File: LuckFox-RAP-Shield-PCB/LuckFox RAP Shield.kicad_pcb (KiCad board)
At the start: 2 copper layers, 21.3 x 28.4 mm, 4 parts, among them J1 LuckFox_Pico_Mini_Connector, J2 External_5V_Input_from_Buck_M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, U2 W5500_Ethernet_Module_DNP_on_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

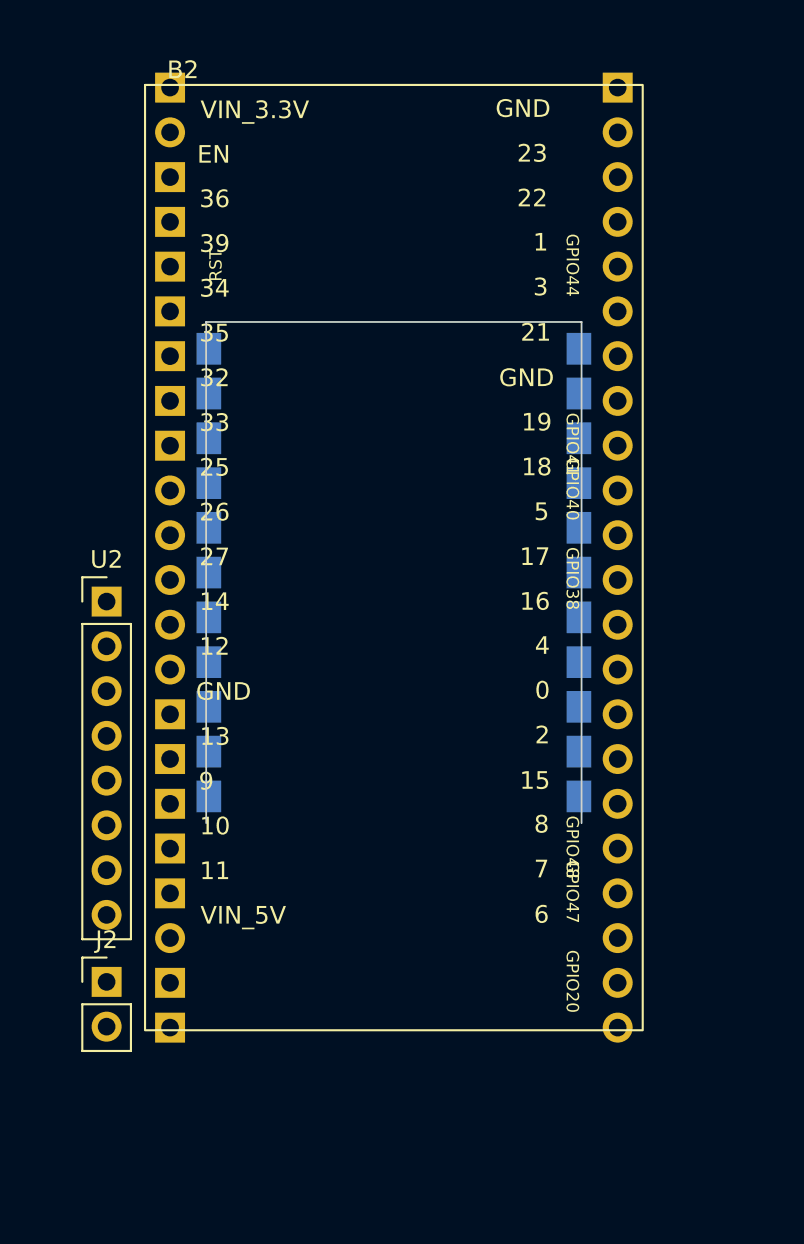
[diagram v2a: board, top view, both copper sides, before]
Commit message: Re-center J1 for the corrected LuckFox footprint dimensions
J1 local center shifted to (10.5, 13.4) with the new 21x26.8mm body.
Re-centered at (124.8, 96.04) using B2's current position; also
picked up that J1 had moved again in your own session.
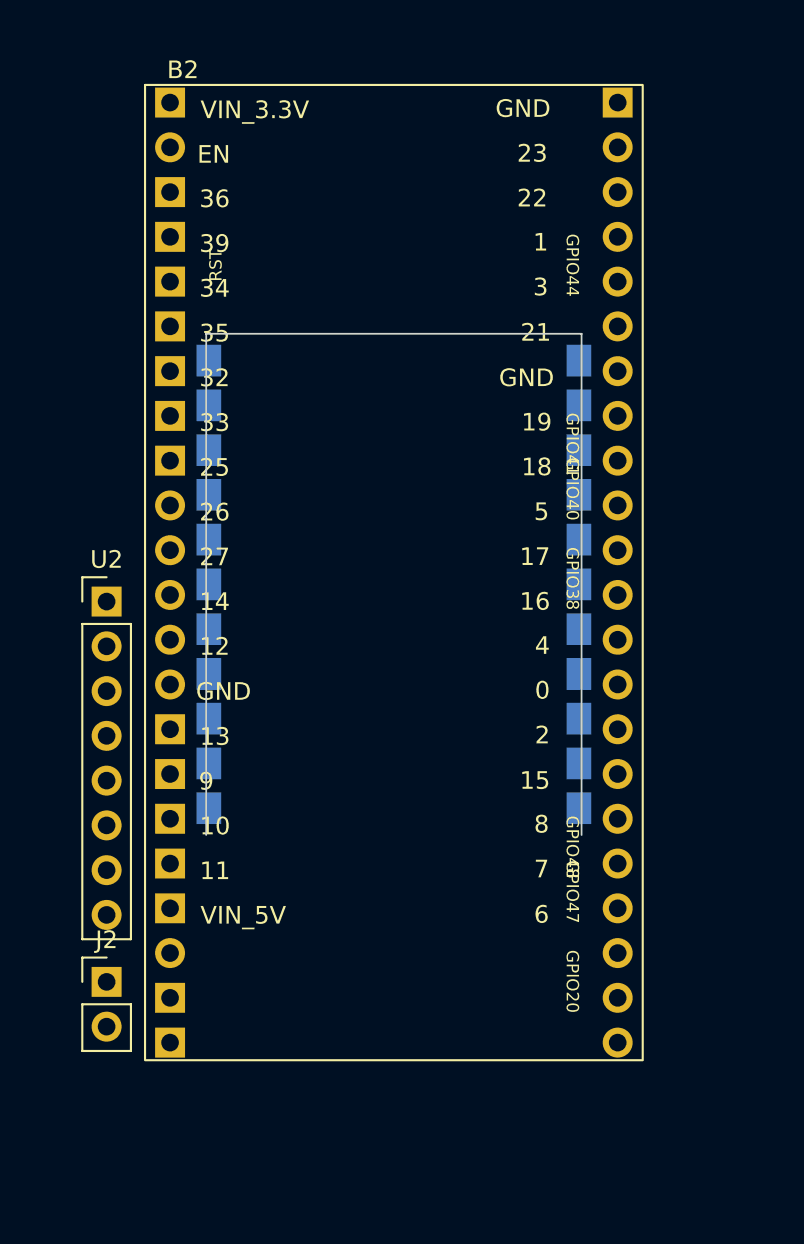
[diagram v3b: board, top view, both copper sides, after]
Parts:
- moved J1 0.67 mm to (124.8, 96.0)
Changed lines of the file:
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@@
 		(layer "F.Cu")
 		(at 121.33 81.92)
-		(descr "Real ESP32-S3-WROOM-1 DevKitC-1 dual-USB-C variant, 44 pins (22/row), 2.54mm pitch, 25.40mm row spacing (1.27mm inset from each edge on a 27.94mm-wide board). Pin labels and this shield's schematic-pin-number mapping are per the board's own silkscreen GPIO numbers -- confirmed against a full pinout diagram. Board length equals the pin-to-pin span exactly (53.34mm, 21 gaps x 2.54mm), zero top/bottom margin, per direct user measurement -- first pin row is flush with the top edge, last pin row flush with the bottom edge.")
+		(descr "Real ESP32-S3-WROOM-1 DevKitC-1 dual-USB-C variant, 44 pins (22/row), 2.54mm pitch, 25.40mm row spacing (1.27mm inset from each edge on a 27.94mm-wide board). Pin labels and this shield's schematic-pin-number mapping are per the board's own silkscreen GPIO numbers -- confirmed against a full pinout diagram. Board length is the pin-to-pin span (53.34mm, 21 gaps x 2.54mm, per direct user measurement) plus 0.85mm margin on each end (half the 1.7mm pad size) so the through-hole pads are physically whole rather than clipped by the board edge -- this is a normal pin-header board, not castellated.")
 		(property "Reference" "B2"
 			(at 2 -1 0)
@@
 		(fp_rect
 			(start -0.15 -0.15)
-			(end 28.09 53.49)
+			(end 28.09 55.19)
 			(stroke
 				(width 0.12)
@@
 		(fp_rect
 			(start -0.4 -0.4)
-			(end 28.34 53.74)
+			(end 28.34 55.44)
 			(stroke
 				(width 0.05)
@@
 		(fp_rect
 			(start 0 0)
-			(end 27.94 53.34)
+			(end 27.94 55.04)
 			(stroke
 				(width 0.1)
@@
 		)
 		(pad "1" thru_hole rect
-			(at 1.27 50.8 90)
+			(at 1.27 51.65 90)
 			(size 1.7 1.7)
 			(drill 1)
@@
 		)
 		(pad "2" thru_hole rect
-			(at 1.27 0 90)
+			(at 1.27 0.85 90)
 			(size 1.7 1.7)
 			(drill 1)
@@
 		)
 		(pad "3" thru_hole rect
-			(at 1.27 53.34 90)
+			(at 1.27 54.19 90)
 			(size 1.7 1.7)
 			(drill 1)
@@
 		)
 		(pad "3V3_B" thru_hole circle
-			(at 1.27 2.54 90)
+			(at 1.27 3.39 90)
 			(size 1.7 1.7)
 			(drill 1)
@@
 		)
 		(pad "4" thru_hole rect
-			(at 1.27 5.08 90)
+			(at 1.27 5.93 90)
 			(size 1.7 1.7)
 			(drill 1)
@@
 		)
 		(pad "5" thru_hole rect
-			(at 1.27 7.62 90)
+			(at 1.27 8.47 90)
 			(size 1.7 1.7)
 			(drill 1)
@@
 		)
 		(pad "6" thru_hole rect
-			(at 1.27 10.16 90)
+			(at 1.27 11.01 90)
 			(size 1.7 1.7)
 			(drill 1)
@@
 		)
 		(pad "7" thru_hole rect
-			(at 1.27 12.7 90)
+			(at 1.27 13.55 90)
 			(size 1.7 1.7)
 			(drill 1)
@@
 		)
 		(pad "8" thru_hole rect
-			(at 1.27 15.24 90)
+			(at 1.27 16.09 90)
 			(size 1.7 1.7)
 			(drill 1)
@@
 		)
 		(pad "9" thru_hole rect
-			(at 1.27 35.56 90)
+			(at 1.27 36.41 90)
 			(size 1.7 1.7)
 			(drill 1)
@@
 		)
 		(pad "10" thru_hole rect
-			(at 1.27 38.1 90)
+			(at 1.27 38.95 90)
 			(size 1.7 1.7)
 			(drill 1)
@@
 		)
 		(pad "11" thru_hole rect
-			(at 1.27 40.64 90)
+			(at 1.27 41.49 90)
 			(size 1.7 1.7)
 			(drill 1)
@@
 		)
 		(pad "12" thru_hole rect
-			(at 1.27 43.18 90)
+			(at 1.27 44.03 90)
 			(size 1.7 1.7)
 			(drill 1)
@@
 		)
 		(pad "13" thru_hole rect
-			(at 1.27 45.72 90)
+			(at 1.27 46.57 90)
 			(size 1.7 1.7)
 			(drill 1)
@@
 		)
 		(pad "14" thru_hole rect
-			(at 1.27 17.78 90)
+			(at 1.27 18.63 90)
 			(size 1.7 1.7)
 			(drill 1)
@@
 		)
 		(pad "15" thru_hole rect
-			(at 1.27 20.32 90)
+			(at 1.27 21.17 90)
 			(size 1.7 1.7)
 			(drill 1)
@@
 		)
 		(pad "16" thru_hole rect
-			(at 26.67 0 270)
+			(at 26.67 0.85 270)
 			(size 1.7 1.7)
 			(drill 1)
@@
 		)
 		(pad "GND_C" thru_hole circle
-			(at 26.67 50.8 270)
+			(at 26.67 51.65 270)
 			(size 1.7 1.7)
 			(drill 1)
@@
 		)
 		(pad "GND_D" thru_hole circle
-			(at 26.67 53.34 270)
+			(at 26.67 54.19 270)
 			(size 1.7 1.7)
 			(drill 1)
@@
 		)
 		(pad "GPIO0" thru_hole circle
-			(at 26.67 33.02 270)
+			(at 26.67 33.87 270)
 			(size 1.7 1.7)
 			(drill 1)
@@
 		)
 		(pad "GPIO1" thru_hole circle
-			(at 26.67 7.62 270)
+			(at 26.67 8.47 270)
 			(size 1.7 1.7)
 			(drill 1)
@@
 		)
 		(pad "GPIO2" thru_hole circle
-			(at 26.67 10.16 270)
+			(at 26.67 11.01 270)
 			(size 1.7 1.7)
 			(drill 1)
@@
 		)
 		(pad "GPIO3" thru_hole circle
-			(at 1.27 30.48 90)
+			(at 1.27 31.33 90)
 			(size 1.7 1.7)
 			(drill 1)
@@
 		)
 		(pad "GPIO8" thru_hole circle
-			(at 1.27 27.94 90)
+			(at 1.27 28.79 90)
 			(size 1.7 1.7)
 			(drill 1)
@@
 		)
 		(pad "GPIO14" thru_hole circle
-			(at 1.27 48.26 90)
+			(at 1.27 49.11 90)
 			(size 1.7 1.7)
 			(drill 1)
@@
 		)
 		(pad "GPIO17" thru_hole circle
-			(at 1.27 22.86 90)
+			(at 1.27 23.71 90)
 			(size 1.7 1.7)
 			(drill 1)
@@
 		)
 		(pad "GPIO18" thru_hole circle
-			(at 1.27 25.4 90)
+			(at 1.27 26.25 90)
 			(size 1.7 1.7)
 			(drill 1)
@@
 		)
 		(pad "GPIO19" thru_hole circle
-			(at 26.67 48.26 270)
+			(at 26.67 49.11 270)
 			(size 1.7 1.7)
 			(drill 1)
@@
 		)
 		(pad "GPIO20" thru_hole circle
-			(at 26.67 45.72 270)
+			(at 26.67 46.57 270)
 			(size 1.7 1.7)
 			(drill 1)
@@
 		)
 		(pad "GPIO21" thru_hole circle
-			(at 26.67 43.18 270)
+			(at 26.67 44.03 270)
 			(size 1.7 1.7)
 			(drill 1)
@@
 		)
 		(pad "GPIO35" thru_hole circle
-			(at 26.67 30.48 270)
+			(at 26.67 31.33 270)
 			(size 1.7 1.7)
 			(drill 1)
@@
 		)
 		(pad "GPIO36" thru_hole circle
-			(at 26.67 27.94 270)
+			(at 26.67 28.79 270)
 			(size 1.7 1.7)
 			(drill 1)
@@
 		)
 		(pad "GPIO37" thru_hole circle
-			(at 26.67 25.4 270)
+			(at 26.67 26.25 270)
 			(size 1.7 1.7)
 			(drill 1)
@@
 		)
 		(pad "GPIO38" thru_hole circle
-			(at 26.67 22.86 270)
+			(at 26.67 23.71 270)
 			(size 1.7 1.7)
 			(drill 1)
@@
 		)
 		(pad "GPIO39" thru_hole circle
-			(at 26.67 20.32 270)
+			(at 26.67 21.17 270)
 			(size 1.7 1.7)
 			(drill 1)
@@
 		)
 		(pad "GPIO40" thru_hole circle
-			(at 26.67 17.78 270)
+			(at 26.67 18.63 270)
 			(size 1.7 1.7)
 			(drill 1)
@@
 		)
 		(pad "GPIO41" thru_hole circle
-			(at 26.67 15.24 270)
+			(at 26.67 16.09 270)
 			(size 1.7 1.7)
 			(drill 1)
@@
 		)
 		(pad "GPIO42" thru_hole circle
-			(at 26.67 12.7 270)
+			(at 26.67 13.55 270)
 			(size 1.7 1.7)
 			(drill 1)
@@
 		)
 		(pad "GPIO43" thru_hole circle
-			(at 26.67 2.54 270)
+			(at 26.67 3.39 270)
 			(size 1.7 1.7)
 			(drill 1)
@@
 		)
 		(pad "GPIO44" thru_hole circle
-			(at 26.67 5.08 270)
+			(at 26.67 5.93 270)
 			(size 1.7 1.7)
 			(drill 1)
@@
 		)
 		(pad "GPIO45" thru_hole circle
-			(at 26.67 35.56 270)
+			(at 26.67 36.41 270)
 			(size 1.7 1.7)
 			(drill 1)
@@
 		)
 		(pad "GPIO46" thru_hole circle
-			(at 1.27 33.02 90)
+			(at 1.27 33.87 90)
 			(size 1.7 1.7)
 			(drill 1)
@@
 		)
 		(pad "GPIO47" thru_hole circle
-			(at 26.67 40.64 270)
+			(at 26.67 41.49 270)
 			(size 1.7 1.7)
 			(drill 1)
@@
 		)
 		(pad "GPIO48" thru_hole circle
-			(at 26.67 38.1 270)
+			(at 26.67 38.95 270)
 			(size 1.7 1.7)
 			(drill 1)
@@
 	(footprint "footprints:LuckFox_Pico_Mini"
 		(layer "B.Cu")
-		(at 124.8 95.37)
+		(at 124.8 96.04)
 		(descr "Cutout + edge-castellation mount for LuckFox Pico Mini, MIRRORED (component side, incl. camera FPC connector, faces AWAY from the shield -- accessible from outside once assembled) -- module nests underneath the shield through this slot. U-shaped opening: enclosed on left/right/top, OPEN on the bottom edge (the USB-C end, post-mirror) so the module's USB-C connector can extend past the shield's own board edge. The open side only works if this footprint is positioned so that opening actually reaches your board's real outer edge -- it is not automatically merged with your board outline. 22 castellated edge pads lap-solder directly to the pads here -- no header/socket. Cutout sized to LuckFox's 21.00x28.14mm outline plus 0.15mm clearance per side; pads centered on LuckFox's nominal edge line (2.54mm pitch, 17.78mm row spacing, per LuckFox's official mechanical drawing) so they straddle the routed slot edge. Pin-row order is reversed vs the unmirrored version: real pin 11/12 (camera-connector end) are now at the top (y=1.37), real pin 1/22 (USB-C end) now at the bottom (y=26.77). Confirm the 0.15mm clearance and pad size against your fab house's minimum slot/annular tolerances before ordering.")
 		(property "Reference" "J1"

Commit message: Readjust Luckfox Pico Mini decorative outline on PCB
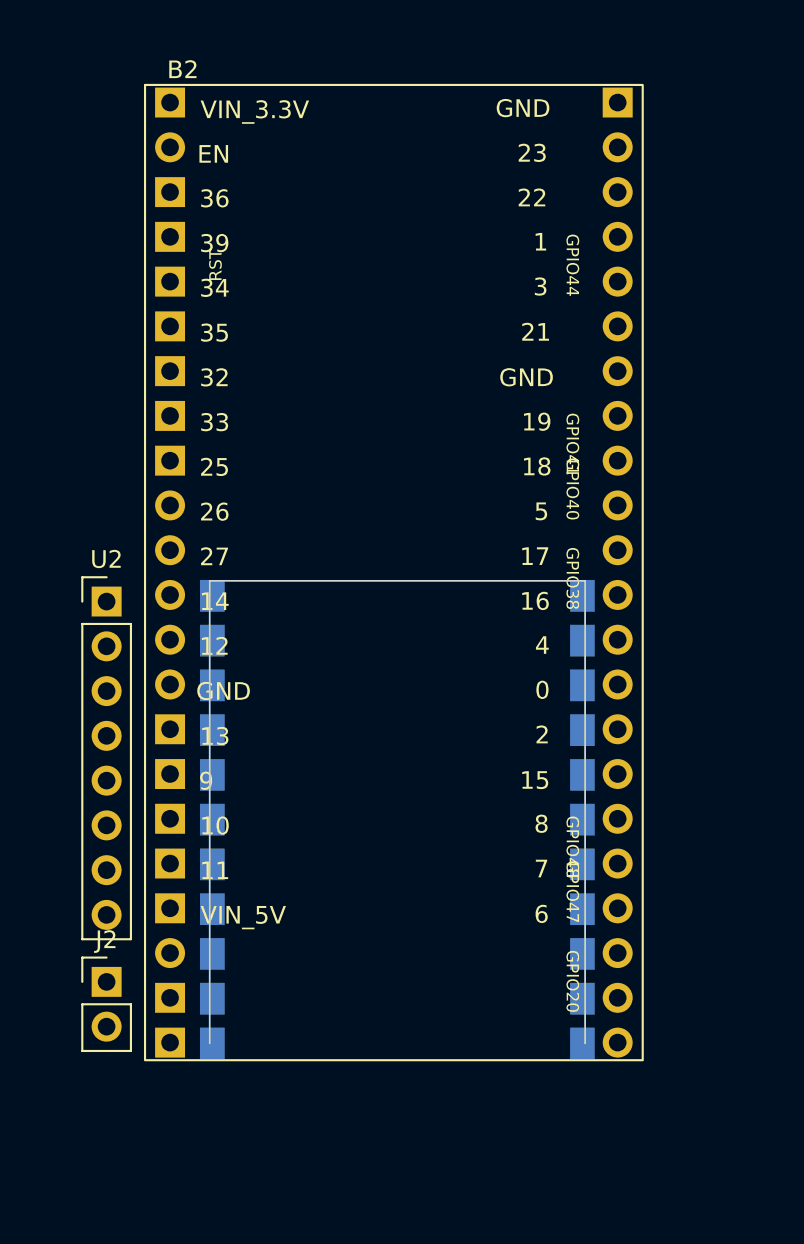
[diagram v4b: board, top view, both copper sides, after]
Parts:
- moved J1 14.0 mm to (125.0, 110.1)
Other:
- board size 21.3 x 28.4 mm -> 21.3 x 26.2 mm
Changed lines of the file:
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@@
 		(sheetname "/")
 		(sheetfile "LuckFox RAP Shield.kicad_sch")
-		(units
-			(unit
-				(name "A")
-				(pins "1" "2" "3" "4" "5" "6" "7" "8")
-			)
-		)
 		(attr through_hole)
 		(duplicate_pad_numbers_are_jumpers no)
@@
 		(sheetname "/")
 		(sheetfile "LuckFox RAP Shield.kicad_sch")
-		(units
-			(unit
-				(name "A")
-				(pins "1" "2")
-			)
-		)
 		(attr through_hole)
 		(duplicate_pad_numbers_are_jumpers no)
@@
 	(footprint "footprints:LuckFox_Pico_Mini"
 		(layer "B.Cu")
-		(at 124.8 96.04)
-		(descr "Cutout + edge-castellation mount for LuckFox Pico Mini, MIRRORED (component side, incl. camera FPC connector, faces AWAY from the shield -- accessible from outside once assembled) -- module nests underneath the shield through this slot. U-shaped opening: enclosed on left/right/top, OPEN on the bottom edge (the USB-C end, post-mirror) so the module's USB-C connector can extend past the shield's own board edge. The open side only works if this footprint is positioned so that opening actually reaches your board's real outer edge -- it is not automatically merged with your board outline. 22 castellated edge pads lap-solder directly to the pads here -- no header/socket. Cutout sized to LuckFox's 21.00x28.14mm outline plus 0.15mm clearance per side; pads centered on LuckFox's nominal edge line (2.54mm pitch, 17.78mm row spacing, per LuckFox's official mechanical drawing) so they straddle the routed slot edge. Pin-row order is reversed vs the unmirrored version: real pin 11/12 (camera-connector end) are now at the top (y=1.37), real pin 1/22 (USB-C end) now at the bottom (y=26.77). Confirm the 0.15mm clearance and pad size against your fab house's minimum slot/annular tolerances before ordering.")
+		(at 125 110.06)
+		(descr "Cutout + edge-castellation mount for LuckFox Pico Mini, MIRRORED (component side, incl. camera FPC connector, faces AWAY from the shield -- accessible from outside once assembled) -- module nests underneath the shield through this slot. Board length = the measured pin-to-pin span (25.4mm, 10 gaps x 2.54mm) plus 0.7mm margin on each end (half the 1.4mm pad height) so the top/bottom-row pads aren't clipped by the board edge -- only the left/right edges are meant to be castellated, per the module's own design. U-shaped opening: enclosed on left/right/top, OPEN on the bottom edge (the USB-C end, post-mirror) so the module's USB-C connector can extend past the shield's own board edge. The left/right enclosing walls stop exactly at the last pin row (y=26.1, pin 1/22) rather than extending through the bottom margin zone -- that margin only exists to keep the pad copper whole, not to add extra enclosed material on the open side. The open side only works if this footprint is positioned so that opening actually reaches your board's real outer edge -- it is not automatically merged with your board outline. 22 castellated edge pads lap-solder directly to the pads here -- no header/socket. Pads centered on LuckFox's nominal edge line (2.54mm pitch, 17.78mm row spacing, per LuckFox's official mechanical drawing) so they straddle the routed slot edge on the left/right. Pin-row order is reversed vs the unmirrored version: real pin 11/12 (camera-connector end) are now at the top (y=0.7), real pin 1/22 (USB-C end) now at the bottom (y=26.1). Confirm the margin/pad size against your fab house's minimum slot/annular tolerances before ordering.")
 		(property "Reference" "J1"
 			(at 2 -1.5 0)
@@
 		)
 		(fp_line
-			(start -0.15 28.29)
+			(start -0.15 26.1)
 			(end -0.15 -0.15)
 			(stroke
@@
 		(fp_line
 			(start 21.15 -0.15)
-			(end 21.15 28.29)
+			(end 21.15 26.1)
 			(stroke
 				(width 0.1)
@@
 		(fp_rect
 			(start -1 -1)
-			(end 22 29.14)
+			(end 22 26.1)
 			(stroke
 				(width 0.05)
@@
 		(fp_rect
 			(start 0 0)
-			(end 21 28.14)
+			(end 21 26.1)
 			(stroke
 				(width 0.1)
@@
 		)
 		(pad "1" smd rect
-			(at 0 26.77 90)
+			(at 0 26.1 90)
 			(size 1.8 1.4)
 			(layers "B.Cu" "B.Mask" "B.Paste")
@@
 		)
 		(pad "2" smd rect
-			(at 0 24.23 90)
+			(at 0 23.56 90)
 			(size 1.8 1.4)
 			(layers "B.Cu" "B.Mask" "B.Paste")
@@
 		)
 		(pad "3" smd rect
-			(at 0 21.69 90)
+			(at 0 21.02 90)
 			(size 1.8 1.4)
 			(layers "B.Cu" "B.Mask" "B.Paste")
@@
 		)
 		(pad "4" smd rect
-			(at 0 19.15 90)
+			(at 0 18.48 90)
 			(size 1.8 1.4)
 			(layers "B.Cu" "B.Mask" "B.Paste")
@@
 		)
 		(pad "5" smd rect
-			(at 0 16.61 90)
+			(at 0 15.94 90)
 			(size 1.8 1.4)
 			(layers "B.Cu" "B.Mask" "B.Paste")
@@
 		)
 		(pad "6" smd rect
-			(at 0 14.07 90)
+			(at 0 13.4 90)
 			(size 1.8 1.4)
 			(layers "B.Cu" "B.Mask" "B.Paste")
@@
 		)
 		(pad "7" smd rect
-			(at 0 11.53 90)
+			(at 0 10.86 90)
 			(size 1.8 1.4)
 			(layers "B.Cu" "B.Mask" "B.Paste")
@@
 		)
 		(pad "8" smd rect
-			(at 0 8.99 90)
+			(at 0 8.32 90)
 			(size 1.8 1.4)
 			(layers "B.Cu" "B.Mask" "B.Paste")
@@
 		)
 		(pad "9" smd rect
-			(at 0 6.45 90)
+			(at 0 5.78 90)
 			(size 1.8 1.4)
 			(layers "B.Cu" "B.Mask" "B.Paste")
@@
 		)
 		(pad "10" smd rect
-			(at 0 3.91 90)
+			(at 0 3.24 90)
 			(size 1.8 1.4)
 			(layers "B.Cu" "B.Mask" "B.Paste")
@@
 		)
 		(pad "11" smd rect
-			(at 0 1.37 90)
+			(at 0 0.7 90)
 			(size 1.8 1.4)
 			(layers "B.Cu" "B.Mask" "B.Paste")
@@
 		)
 		(pad "12" smd rect
-			(at 21 1.37 90)
+			(at 21 0.7 90)
 			(size 1.8 1.4)
 			(layers "B.Cu" "B.Mask" "B.Paste")
@@
 		)
 		(pad "13" smd rect
-			(at 21 3.91 90)
+			(at 21 3.24 90)
 			(size 1.8 1.4)
 			(layers "B.Cu" "B.Mask" "B.Paste")
@@
 		)
 		(pad "14" smd rect
-			(at 21 6.45 90)
+			(at 21 5.78 90)
 			(size 1.8 1.4)
 			(layers "B.Cu" "B.Mask" "B.Paste")
@@
 		)
 		(pad "15" smd rect
-			(at 21 8.99 90)
+			(at 21 8.32 90)
 			(size 1.8 1.4)
 			(layers "B.Cu" "B.Mask" "B.Paste")
@@
 		)
 		(pad "16" smd rect
-			(at 21 11.53 90)
+			(at 21 10.86 90)
 			(size 1.8 1.4)
 			(layers "B.Cu" "B.Mask" "B.Paste")
@@
 		)
 		(pad "17" smd rect
-			(at 21 14.07 90)
+			(at 21 13.4 90)
 			(size 1.8 1.4)
 			(layers "B.Cu" "B.Mask" "B.Paste")
@@
 		)
 		(pad "18" smd rect
-			(at 21 16.61 90)
+			(at 21 15.94 90)
 			(size 1.8 1.4)
 			(layers "B.Cu" "B.Mask" "B.Paste")
@@
 		)
 		(pad "19" smd rect
-			(at 21 19.15 90)
+			(at 21 18.48 90)
 			(size 1.8 1.4)
 			(layers "B.Cu" "B.Mask" "B.Paste")
@@
 		)
 		(pad "20" smd rect
-			(at 21 21.69 90)
+			(at 21 21.02 90)
 			(size 1.8 1.4)
 			(layers "B.Cu" "B.Mask" "B.Paste")
@@
 		)
 		(pad "21" smd rect
-			(at 21 24.23 90)
+			(at 21 23.56 90)
 			(size 1.8 1.4)
 			(layers "B.Cu" "B.Mask" "B.Paste")
@@
 		)
 		(pad "22" smd rect
-			(at 21 26.77 90)
-			(size 1.8 1.4)
-			(layers "B.Cu" "B.Mask" "B.Paste")
+			(at 21 26.1 90)
+			(size 1.8 1.4)
+			(layers "B.Cu" "B.Mask" "B.Paste")
